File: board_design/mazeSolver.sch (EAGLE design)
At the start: 53 parts, among them IC1 L293DD, IC2 7805TV, IC3 CP2101, Q1 BC547, Q2 BC547, U1 MPU-9250, U2 AP1509-SOP8L, U3 ESP-WROOM-32, U4 GY-521MPU6050

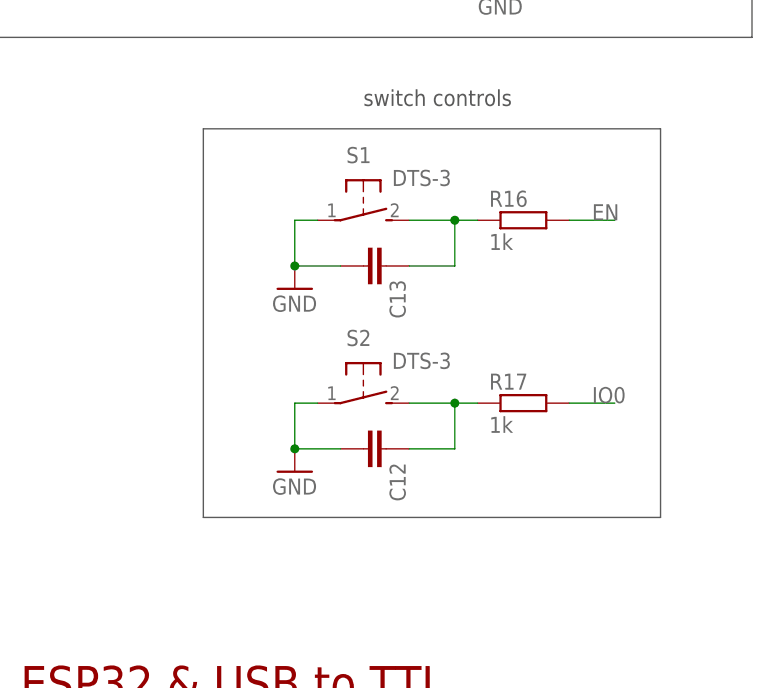
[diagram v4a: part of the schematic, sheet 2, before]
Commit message: Components placement
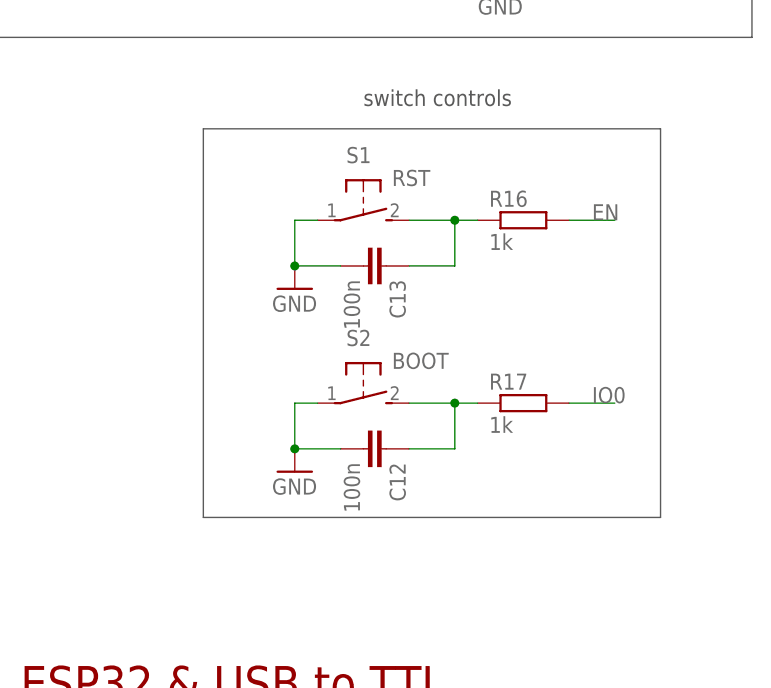
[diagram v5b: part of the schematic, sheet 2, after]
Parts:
- C12, C13: value (none) -> 100n
- S1: value DTS-3 -> RST
- S2: value DTS-3 -> BOOT
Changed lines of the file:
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@@
 <part name="GND20" library="supply1" library_urn="urn:adsk.eagle:library:371" deviceset="GND" device=""/>
 <part name="R15" library="rcl" library_urn="urn:adsk.eagle:library:334" deviceset="R-EU_" device="R1206" package3d_urn="urn:adsk.eagle:package:23540/2" value="10k"/>
-<part name="S1" library="switch-tact" deviceset="DTS-3" device=""/>
-<part name="S2" library="switch-tact" deviceset="DTS-3" device=""/>
+<part name="S1" library="switch-tact" deviceset="DTS-3" device="" value="RST"/>
+<part name="S2" library="switch-tact" deviceset="DTS-3" device="" value="BOOT"/>
 <part name="R16" library="rcl" library_urn="urn:adsk.eagle:library:334" deviceset="R-EU_" device="R1206" package3d_urn="urn:adsk.eagle:package:23540/2" value="1k"/>
 <part name="R17" library="rcl" library_urn="urn:adsk.eagle:library:334" deviceset="R-EU_" device="R1206" package3d_urn="urn:adsk.eagle:package:23540/2" value="1k"/>
-<part name="C12" library="rcl" library_urn="urn:adsk.eagle:library:334" deviceset="C-EU" device="C1206" package3d_urn="urn:adsk.eagle:package:23618/2"/>
-<part name="C13" library="rcl" library_urn="urn:adsk.eagle:library:334" deviceset="C-EU" device="C1206" package3d_urn="urn:adsk.eagle:package:23618/2"/>
+<part name="C12" library="rcl" library_urn="urn:adsk.eagle:library:334" deviceset="C-EU" device="C1206" package3d_urn="urn:adsk.eagle:package:23618/2" value="100n"/>
+<part name="C13" library="rcl" library_urn="urn:adsk.eagle:library:334" deviceset="C-EU" device="C1206" package3d_urn="urn:adsk.eagle:package:23618/2" value="100n"/>
 <part name="GND21" library="supply1" library_urn="urn:adsk.eagle:library:371" deviceset="GND" device=""/>
 <part name="GND26" library="supply1" library_urn="urn:adsk.eagle:library:371" deviceset="GND" device=""/>

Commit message: PCB Design
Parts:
- removed S1: RST, switch-tact:DTS-3
- removed S2: BOOT, switch-tact:DTS-3
- added U5: RST, Switches:4-1437565-1
- added U6: BOOT, Switches:4-1437565-1
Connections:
- net GND: now also U5.1, U5.2, U6.1, U6.2; no longer S1.1, S2.1
- net N$14: now also U5.3, U5.4; no longer S1.2
- net N$15: now also U6.3, U6.4; no longer S2.2
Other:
- moved on the sheet: C12, R16, R17

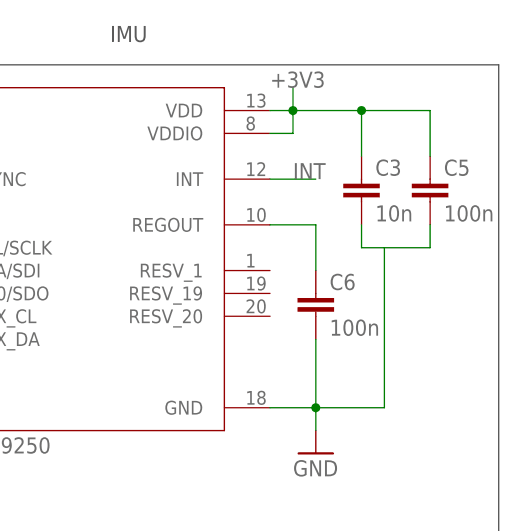
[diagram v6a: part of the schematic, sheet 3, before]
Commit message: DRC Checks are passing
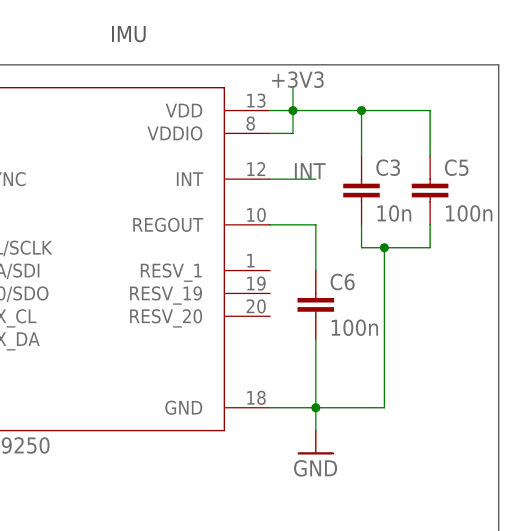
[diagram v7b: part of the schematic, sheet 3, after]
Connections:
- removed net DSR: IC3.DSR
